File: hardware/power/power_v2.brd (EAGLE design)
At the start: 92 x 92 mm, 43 parts, among them J1 FASTON1289_ST, J2 FASTON1289_ST, J3 12v, J4 5v, J5 XT30PW-F, J6 XT30PW-F, J7 XT30PW-F, J8 XT30PW-F, Q1 MMBT5401L, Q2 PSMN1R0-40YSH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

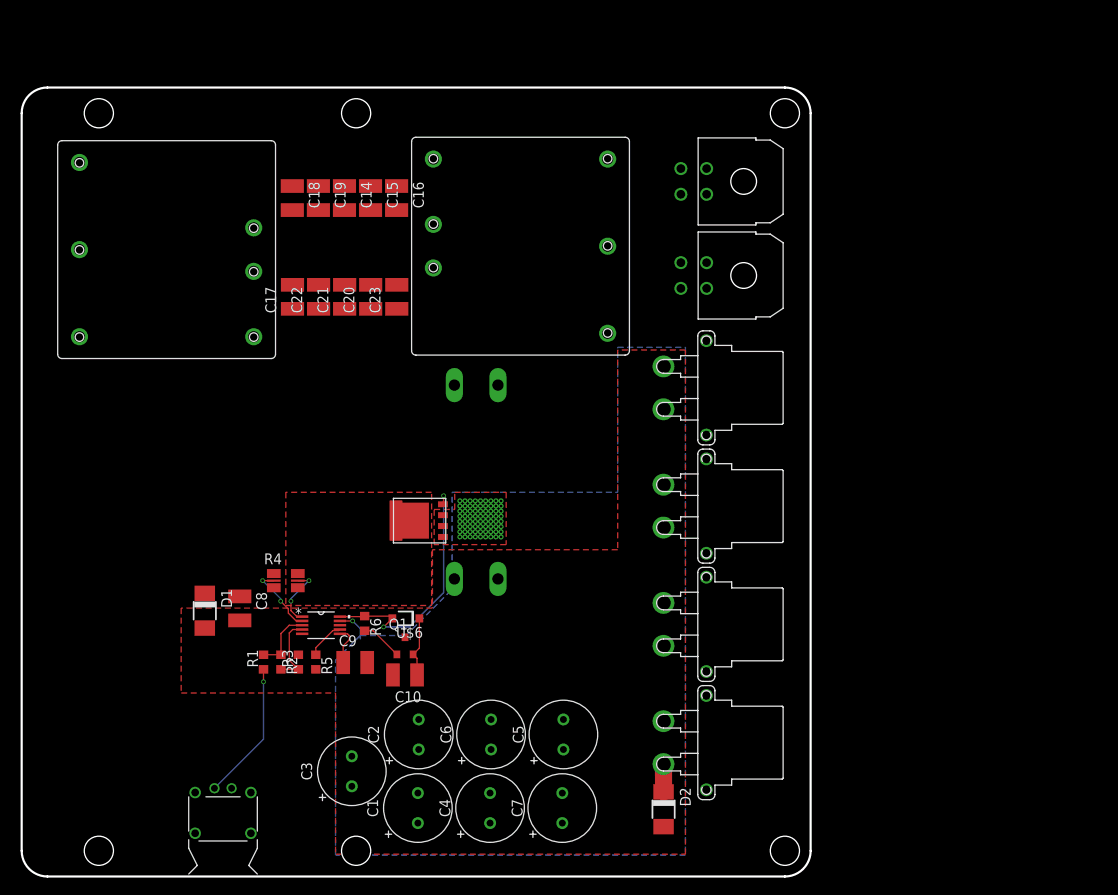
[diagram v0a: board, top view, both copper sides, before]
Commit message: Going to rework power plane v2
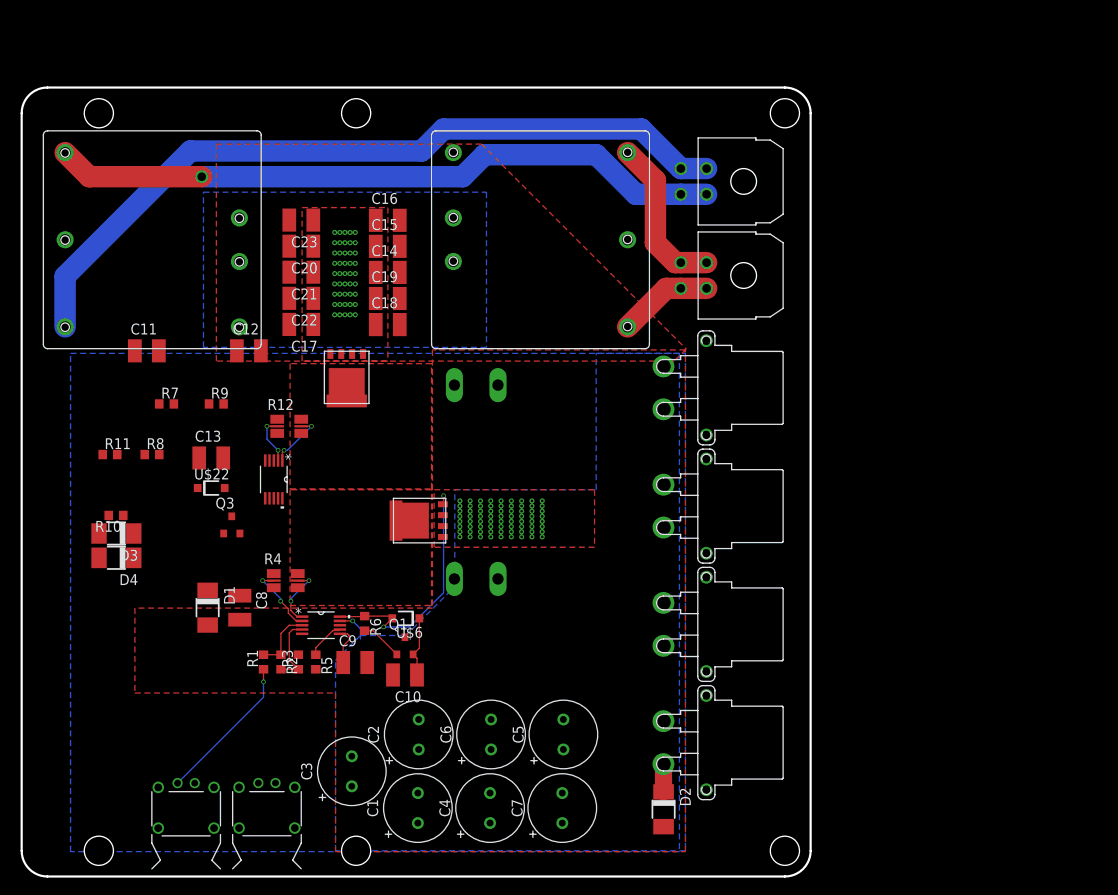
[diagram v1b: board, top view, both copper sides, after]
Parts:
- added C11: 0.01uF, timlib:C1210
- added C12: 2.2n, timlib:C1210
- added C13: 16nF, timlib:C1210
- added D3: SMAJ30A, timlib:DO-214AC
- added D4: SK510A-LTP, timlib:DO-214AC
- added Q3: MMBT5401L, timlib:SOT23-3
- added Q4: PSMN1R0-40YSH, timlib:LFPAK56E
- added R10: 18.9k, rcl:R0603
- added R11: 18.9, rcl:R0603
- added R12: PMR25HZPFV, timlib:R1210_KELVIN
- added R7: 47.5k, rcl:R0603
- added R8: 3.4k, rcl:R0603
- added R9: 4.32k, rcl:R0603
- added U$13: 2-PIN, timlib:M80-8420242
- added U$14: LM5069_DGS_10, timlib:VSSOP_DGS_10
- added U$22: 1N4148W-7-F, timlib:SOD123
- moved U1 43.6 mm to (60.5, 74.2), turned to 90 degrees
- moved U2 42.9 mm to (15.2, 74.2), turned to 270 degrees
- moved C18 18.5 mm to (42.7, 64.4), turned to 0 degrees
- moved C23 14.3 mm to (32.6, 76.5), turned to 180 degrees
- moved C19 14.2 mm to (42.7, 67.4), turned to 0 degrees
- moved C14 10.0 mm to (42.7, 70.4), turned to 0 degrees
- moved C20 10.0 mm to (32.6, 73.5), turned to 180 degrees
- moved C15 5.98 mm to (42.7, 73.5), turned to 0 degrees
- moved C21 5.81 mm to (32.6, 70.5), turned to 180 degrees
- moved U$26 4.34 mm to (19.2, 10.9)
- moved C17 3.37 mm to (32.6, 64.4), turned to 180 degrees
- moved C16 2.79 mm to (42.7, 76.5), turned to 0 degrees
- moved C22 2.02 mm to (32.6, 67.4), turned to 180 degrees
- moved D1 0.49 mm to (21.7, 31.3)
- moved C8 0.09 mm to (25.4, 31.3)
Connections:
- removed net ISO_GND: U1.P$2, U2.P$2
- new net MOSFET_DRAIN1: Q4.5, R12.2A, R12.2B
- new net N$12: R8.2, R9.1, U$14.4
- new net N$13: R7.1, U$13.2
- new net N$14: Q4.4, R11.1, U$14.10, U$22.A
- new net N$15: R10.1, U$14.7
- new net N$16: C12.1, U$14.6
- new net N$17: C13.1, Q3.E, U$22.C
- new net N$18: Q3.B, R11.2
- new net N$19: R12.1_KELVIN, U$14.2
- new net N$20: R12.2_KELVIN, U$14.1
- new net N$4: R7.2, R8.1, U$14.3
- net +24V_BATT: now also C11.1, D3.C, R12.1A, R12.1B, U$13.1; no longer U1.P$1, U2.P$1
- net +24V_ISO: now also D4.C, Q4.1, Q4.2, Q4.3, U$14.9, U1.P$1, U2.P$1
- net GND_BATT: now also C11.2, C12.2, C13.2, D3.A, D4.A, Q3.C, R10.2, R9.2, U$14.5, U1.P$2, U2.P$2
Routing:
- net 12V_GND: track 0.00 -> 89.7 mm
- net +12VOUT: track 0.00 -> 78.9 mm, vias 0 -> 1
- net 5V_GND: track 0.00 -> 18.8 mm
- net +5VOUT: track 0.00 -> 11.1 mm
- net N$20: track 0.00 -> 6.84 mm, vias 0 -> 2
- net N$19: track 0.00 -> 5.74 mm, vias 0 -> 2
- net N$3: track 16.2 -> 17.4 mm
- added copper zone on layer 16, net +24V_BATT
- added copper zone on layer 1, net +24V_ISO
- added copper zone on layer 16, net +24V_ISO
- added copper zone on layer 1, net MOSFET_DRAIN1

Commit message: Another repeat redo
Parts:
- moved C11 98.8 mm to (107.0, 96.4)
- moved C12 98.8 mm to (118.9, 96.4)
- moved C13 98.8 mm to (114.5, 83.9)
- moved Q3 98.8 mm to (116.9, 76.1)
- moved R10 98.8 mm to (103.4, 77.2)
- moved R11 98.8 mm to (102.7, 84.3)
- moved R7 98.8 mm to (109.3, 90.2)
- moved U$14 98.8 mm to (121.8, 81.4)
- moved U$22 98.8 mm to (114.5, 80.4)
- moved D3 98.8 mm to (103.4, 75.1)
- moved D4 98.8 mm to (103.4, 72.3)
- moved R12 98.8 mm to (123.6, 87.6)
- moved R8 98.8 mm to (107.6, 84.3)
- moved R9 98.8 mm to (115.1, 90.2)
- moved C14 28.6 mm to (14.2, 72.2)
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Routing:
- net 12V_GND: track 89.7 -> 0.00 mm
- net +12VOUT: track 78.9 -> 0.00 mm, vias 1 -> 0
- net N$5: track 28.7 -> 0.00 mm, vias 2 -> 0
- net 5V_GND: track 18.8 -> 0.00 mm
- net N$3: track 17.4 -> 0.00 mm, vias 1 -> 0
- net +5VOUT: track 11.1 -> 0.00 mm
- net N$2: track 8.39 -> 0.00 mm
- net N$1: track 7.38 -> 0.00 mm
- net +24V_LEG: track 7.21 -> 0.00 mm, vias 73 -> 0
- net N$8: track 7.09 -> 0.00 mm
- net N$20: track 6.84 -> 0.00 mm, vias 2 -> 0
- net N$19: track 5.74 -> 0.00 mm, vias 2 -> 0
- net N$9: track 4.89 -> 0.00 mm
- net N$7: track 4.62 -> 0.00 mm
- net N$6: track 4.51 -> 0.00 mm
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- added copper zone on layer 1, net +24V_BATT
- removed copper zone on layer 16, net +24V_BATT
- removed copper zone on layer 16, net +24V_ISO

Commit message: Happy with this layout
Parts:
- removed C11: 0.01uF, timlib:C1210
- removed U$22, U$6: 1N4148W-7-F, timlib:SOD123
- added D5: 1N4148W-7-F, timlib:SOD123
- D3: value SMAJ30A -> 1N4148W-7-F; device timlib:DO-214AC -> timlib:SOD123
- moved C12 129.0 mm to (5.90, 34.1), turned to 180 degrees
- moved C13 118.2 mm to (5.90, 37.3), turned to 180 degrees
- moved Q3 114.4 mm to (10.9, 33.0), turned to 90 degrees
- moved R9 113.3 mm to (12.0, 43.2), turned to 180 degrees
- moved U$14 110.9 mm to (19.0, 39.7)
- moved R12 110.4 mm to (21.1, 46.5), turned to 180 degrees
- moved R7 109.9 mm to (12.0, 39.1)
- moved R8 104.9 mm to (12.0, 41.1)
- moved R11 102.6 mm to (14.5, 31.8), turned to 180 degrees
- moved D3 101.5 mm to (17.7, 20.8), turned to 0 degrees
- moved R10 97.3 mm to (15.0, 36.6)
- moved D4 72.0 mm to (33.4, 89.0)
- moved C3 52.6 mm to (66.6, 56.8)
- moved C8 50.6 mm to (58.4, 38.5)
- moved D1 49.1 mm to (53.1, 38.6)
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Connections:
- net +24V_BATT: no longer C11.1, D3.C
- net GND_BATT: no longer C11.2, D3.A
- net N$14: now also D5.A; no longer U$22.A
- net N$17: now also D5.C; no longer U$22.C
- net N$5: now also D3.A; no longer U$6.A
- net N$8: now also D3.C; no longer U$6.C
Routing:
- net N$14: track 0.00 -> 56.5 mm, vias 0 -> 2
- net +12VOUT: track 0.00 -> 43.6 mm
- net N$5: track 0.00 -> 43.3 mm, vias 0 -> 2
- net +24V_ISO: track 0.00 -> 42.5 mm, vias 0 -> 2
- net +24V_BATT: track 0.00 -> 40.8 mm
- net 12V_GND: track 0.00 -> 38.2 mm
- net N$13: track 0.00 -> 35.8 mm, vias 0 -> 2
- net +24V_LEG: track 0.00 -> 31.6 mm, vias 0 -> 2
- net N$3: track 0.00 -> 31.4 mm, vias 0 -> 4
- net 5V_GND: track 0.00 -> 18.9 mm
- net GND_BATT: track 0.00 -> 17.5 mm, vias 0 -> 87
- net N$7: track 0.00 -> 15.6 mm
- net N$4: track 0.00 -> 13.5 mm, vias 0 -> 2
- net N$1: track 0.00 -> 12.7 mm, vias 0 -> 3
- net N$2: track 0.00 -> 12.4 mm
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- added copper zone on layer 16, net GND_BATT
- removed copper zone on layer 16, net +24V_LEG

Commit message: Flipped terminal tabs
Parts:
- flipped J1 to the bottom
- flipped J2 to the bottom
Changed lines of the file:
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@@
 </layers>
 <board>
-<fusionsync huburn="a.YnVzaW5lc3M6Z21haWwyMjE5MTc" projecturn="a.YnVzaW5lc3M6Z21haWwyMjE5MTcjMjAxOTA2MjkyMDE0MTU5NzY" f3durn="urn:adsk.wipprod:dm.lineage:MB3VqYkNRX6Sa_ecpPTqbA" pcbguid="9dcfff74-9686-4bdf-a14e-dd144a326308" lastpulledtime="2020-01-18T04:37:27Z" lastsyncedchangeguid="ea626e1d-bd38-a2ba-998e-c3714614e30b"/>
+<fusionsync huburn="a.YnVzaW5lc3M6Z21haWwyMjE5MTc" projecturn="a.YnVzaW5lc3M6Z21haWwyMjE5MTcjMjAxOTA2MjkyMDE0MTU5NzY" f3durn="urn:adsk.wipprod:dm.lineage:MB3VqYkNRX6Sa_ecpPTqbA" pcbguid="9dcfff74-9686-4bdf-a14e-dd144a326308" lastpulledtime="2020-01-18T04:37:27Z" lastsyncedchangeguid="4dd21494-0389-bce7-bd1b-602bba9568d1"/>
 <plain>
 <hole x="39" y="89" drill="3.4"/>
@@
 <element name="J7" library="timlib" library_urn="urn:adsk.eagle:library:16152524" package="XT30PW-F" package3d_urn="urn:adsk.eagle:package:16203166/7" value="XT30PW-F" x="81.94" y="29.4" smashed="yes" rot="R270"/>
 <element name="J8" library="timlib" library_urn="urn:adsk.eagle:library:16152524" package="XT30PW-F" package3d_urn="urn:adsk.eagle:package:16203166/7" value="XT30PW-F" x="81.94" y="15.61" smashed="yes" rot="R270"/>
-<element name="J1" library="timlib" library_urn="urn:adsk.eagle:library:16152524" package="FASTON_1289-ST" package3d_urn="urn:adsk.eagle:package:16406409/3" value="FASTON1289_ST" x="53" y="57.3" locked="yes" smashed="yes" rot="R180"/>
-<element name="J2" library="timlib" library_urn="urn:adsk.eagle:library:16152524" package="FASTON_1289-ST" package3d_urn="urn:adsk.eagle:package:16406409/3" value="FASTON1289_ST" x="53" y="34.7" locked="yes" smashed="yes"/>
+<element name="J1" library="timlib" library_urn="urn:adsk.eagle:library:16152524" package="FASTON_1289-ST" package3d_urn="urn:adsk.eagle:package:16406409/3" value="FASTON1289_ST" x="53" y="57.3" locked="yes" smashed="yes" rot="MR180"/>
+<element name="J2" library="timlib" library_urn="urn:adsk.eagle:library:16152524" package="FASTON_1289-ST" package3d_urn="urn:adsk.eagle:package:16406409/3" value="FASTON1289_ST" x="53" y="34.7" locked="yes" smashed="yes" rot="MR0"/>
 <element name="J3" library="timlib" library_urn="urn:adsk.eagle:library:16152524" package="MOLEX_4_RA" package3d_urn="urn:adsk.eagle:package:16152611/3" value="12v" x="86.29" y="81.05" smashed="yes" rot="R90"/>
 <element name="J4" library="timlib" library_urn="urn:adsk.eagle:library:16152524" package="MOLEX_4_RA" package3d_urn="urn:adsk.eagle:package:16152611/3" value="5v" x="86.29" y="70.08" smashed="yes" rot="R90"/>

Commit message: Moved caps around a bit, made traces thicker.
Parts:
- moved C3 50.1 mm to (59.1, 7.26), turned to 270 degrees
- moved C6 41.2 mm to (67.9, 7.26), turned to 270 degrees
- moved D2 27.6 mm to (73.5, 43.7)
- moved C1 25.4 mm to (67.9, 32.4), turned to 270 degrees
- moved C5 17.8 mm to (59.1, 24.0), turned to 270 degrees
- moved C7 8.07 mm to (67.9, 15.6), turned to 270 degrees
- moved C2 8.00 mm to (67.9, 24.0), turned to 270 degrees
- moved C4 7.41 mm to (59.1, 15.6), turned to 270 degrees
- moved C8 0.54 mm to (57.9, 38.3)
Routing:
- net +24V_LEG: track 31.6 -> 32.1 mm

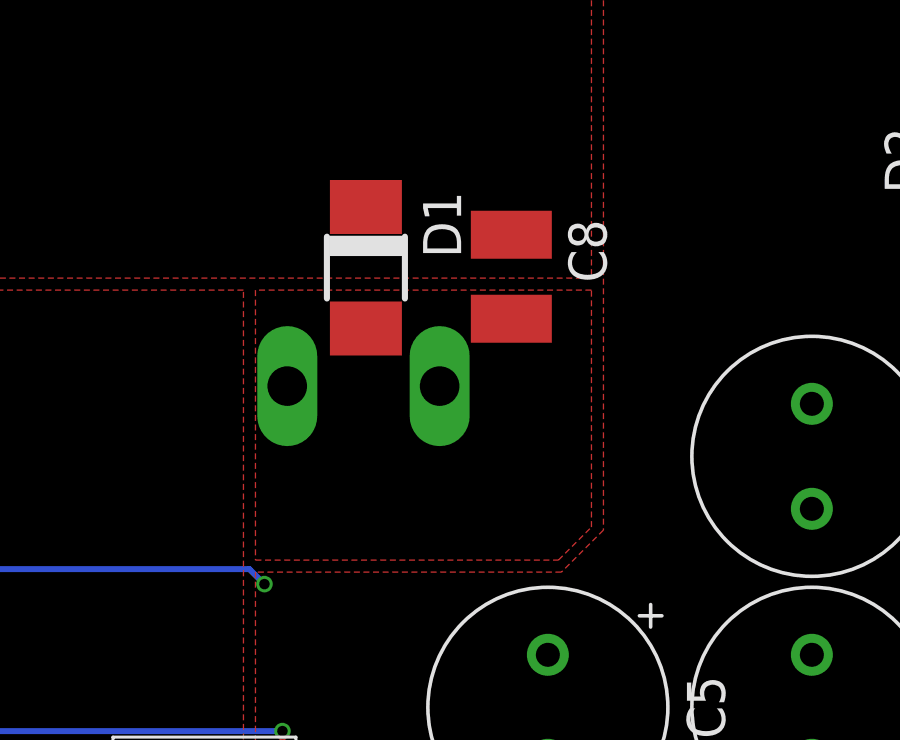
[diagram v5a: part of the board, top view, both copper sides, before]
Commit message: Isolation for planes
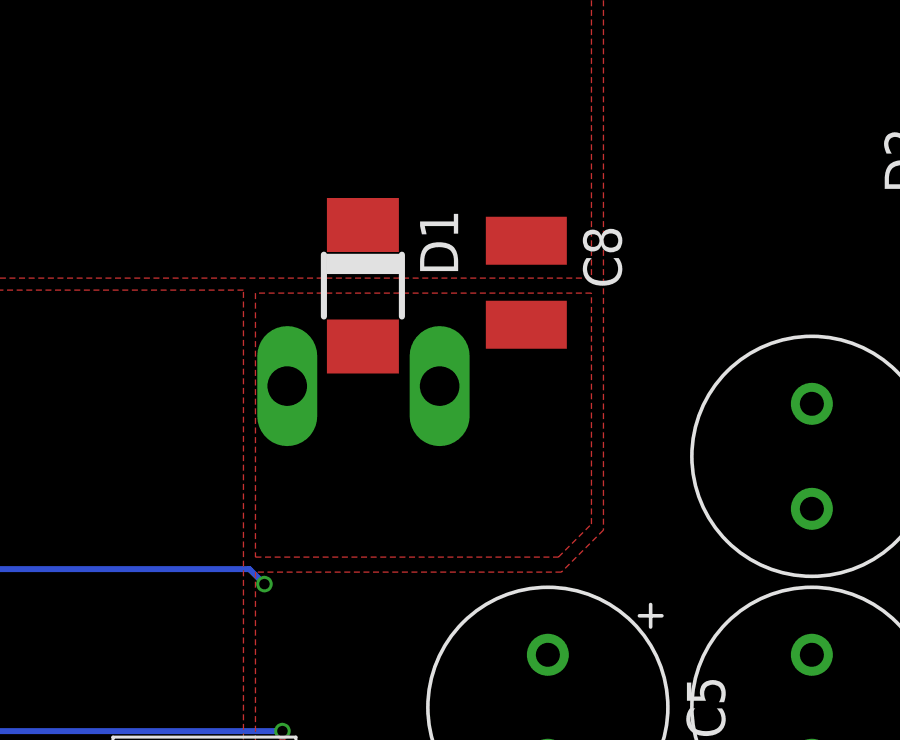
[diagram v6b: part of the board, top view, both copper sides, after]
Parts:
- moved D1 0.61 mm to (53.0, 38.0)
- moved C8 0.54 mm to (58.4, 38.1)
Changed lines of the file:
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@@
 </element>
 <element name="U$1" library="timlib" library_urn="urn:adsk.eagle:library:16152524" package="VSSOP_DGS_10" package3d_urn="urn:adsk.eagle:package:16499421/2" value="LM5069_DGS_10" x="19.1" y="32.19" smashed="yes" rot="R270"/>
-<element name="D1" library="timlib" library_urn="urn:adsk.eagle:library:16152524" package="DO-214AC" package3d_urn="urn:adsk.eagle:package:16356227/6" value="SMAJ30A" x="53.08213125" y="38.645" smashed="yes" rot="R270">
-<attribute name="NAME" x="54.98713125" y="41.185" size="1.27" layer="25" rot="R270"/>
-<attribute name="VALUE" x="49.90713125" y="41.185" size="1.27" layer="27" rot="R270"/>
-</element>
-<element name="C8" library="timlib" library_urn="urn:adsk.eagle:library:16152524" package="C1210" package3d_urn="urn:adsk.eagle:package:23619/2" value="0.01uF" x="57.929996875" y="38.345" smashed="yes" rot="R270">
-<attribute name="NAME" x="59.834996875" y="40.25" size="1.27" layer="25" rot="R270"/>
-<attribute name="VALUE" x="54.754996875" y="40.25" size="1.27" layer="27" rot="R270"/>
+<element name="D1" library="timlib" library_urn="urn:adsk.eagle:library:16152524" package="DO-214AC" package3d_urn="urn:adsk.eagle:package:16356227/6" value="SMAJ30A" x="52.98213125" y="38.045" smashed="yes" rot="R270">
+<attribute name="NAME" x="54.88713125" y="40.585" size="1.27" layer="25" rot="R270"/>
+<attribute name="VALUE" x="49.80713125" y="40.585" size="1.27" layer="27" rot="R270"/>
+</element>
+<element name="C8" library="timlib" library_urn="urn:adsk.eagle:library:16152524" package="C1210" package3d_urn="urn:adsk.eagle:package:23619/2" value="0.01uF" x="58.429996875" y="38.145" smashed="yes" rot="R270">
+<attribute name="NAME" x="60.334996875" y="40.05" size="1.27" layer="25" rot="R270"/>
+<attribute name="VALUE" x="55.254996875" y="40.05" size="1.27" layer="27" rot="R270"/>
 </element>
 <element name="R1" library="rcl" library_urn="urn:adsk.eagle:library:334" package="R0603" package3d_urn="urn:adsk.eagle:package:23555/3" value="47.5k" x="13.61" y="29.2" smashed="yes">
@@
 <contactref element="R12" pad="1B"/>
 <contactref element="R12" pad="1A"/>
-<polygon width="0.3" layer="1" thermals="no" rank="2">
+<polygon width="0.3" layer="1" isolate="0.3" thermals="no" rank="2">
 <vertex x="60.6" y="61"/>
 <vertex x="60.6" y="38.3"/>
@@
 <contactref element="U2" pad="P$2"/>
 <contactref element="U1" pad="P$2"/>
-<polygon width="0.1524" layer="16" thermals="no">
+<polygon width="0.1524" layer="16" isolate="0.5" thermals="no">
 <vertex x="0.8" y="87"/>
 <vertex x="89.1" y="87"/>
@@
 <via x="28.7" y="83.5" extent="1-16" drill="0.35" diameter="0.5"/>
 <via x="28.7" y="84.7" extent="1-16" drill="0.35" diameter="0.5"/>
-<polygon width="0.1524" layer="1" thermals="no" rank="4">
+<polygon width="0.1524" layer="1" isolate="0.3" thermals="no" rank="4">
 <vertex x="2" y="90.1"/>
 <vertex x="36" y="90.1"/>
@@
 <wire x1="12.7" y1="19.6" x2="11.8" y2="19.6" width="0.3" layer="1"/>
 <via x="11.8" y="19.6" extent="1-16" drill="0.35"/>
-<polygon width="0.1524" layer="1" thermals="no">
-<vertex x="49.4" y="28.9"/>
-<vertex x="59.5" y="28.9"/>
-<vertex x="60.6" y="30"/>
-<vertex x="60.6" y="37.9"/>
-<vertex x="49.4" y="37.9"/>
+<polygon width="0.1524" layer="1" isolate="0.3" thermals="no">
+<vertex x="49.4" y="29"/>
+<vertex x="59.5" y="29"/>
+<vertex x="60.6" y="30.1"/>
+<vertex x="60.6" y="37.8"/>
+<vertex x="49.4" y="37.8"/>
 </polygon>
 <wire x1="76.94" y1="45.69" x2="76.935" y2="45.685" width="2.5" layer="1"/>
@@
 <contactref element="R4" pad="2B"/>
 <contactref element="R4" pad="2A"/>
-<polygon width="0.1524" layer="1" thermals="no" rank="3">
+<polygon width="0.1524" layer="1" isolate="0.3" thermals="no" rank="3">
 <vertex x="49" y="13"/>
 <vertex x="49" y="37.9"/>
@@
 <contactref element="C2" pad="1"/>
 <contactref element="C1" pad="1"/>
-<polygon width="0.1524" layer="1" thermals="no">
+<polygon width="0.1524" layer="1" isolate="0.3" thermals="no">
 <vertex x="49.4" y="3.7"/>
 <vertex x="80.3" y="3.7"/>
@@
 <contactref element="Q4" pad="1"/>
 <contactref element="Q4" pad="3"/>
-<polygon width="0.1524" layer="1" thermals="no">
+<polygon width="0.1524" layer="1" isolate="0.3" thermals="no">
 <vertex x="2" y="61.5"/>
 <vertex x="43.3" y="61.5"/>
@@
 <contactref element="R12" pad="2A"/>
 <contactref element="R12" pad="2B"/>
-<polygon width="0.1524" layer="1" thermals="no">
+<polygon width="0.1524" layer="1" isolate="0.3" thermals="no">
 <vertex x="2" y="61"/>
 <vertex x="2" y="44"/>
